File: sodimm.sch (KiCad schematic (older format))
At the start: 1 part, among them J5 2309409-1

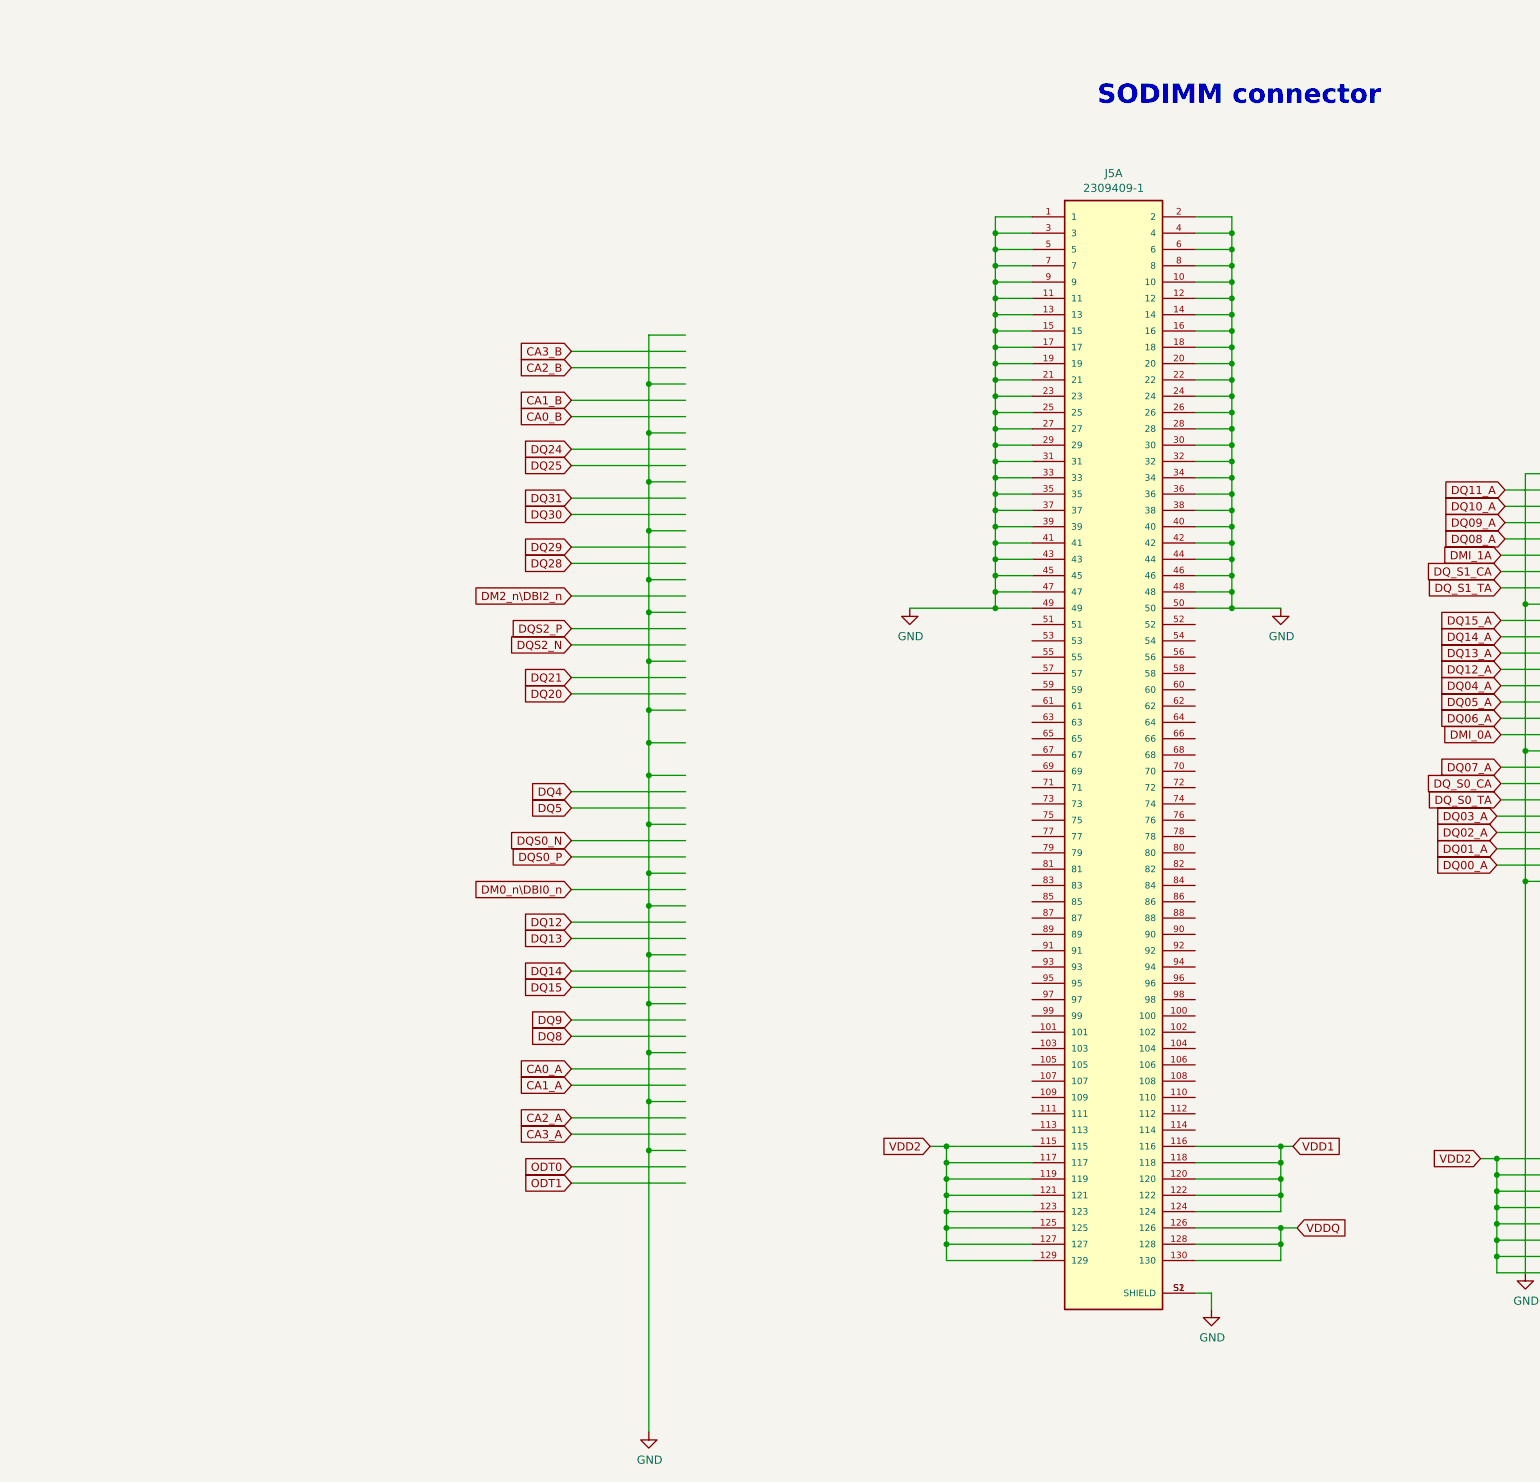
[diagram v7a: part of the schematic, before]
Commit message: Remove redundant signals from the SODIMM
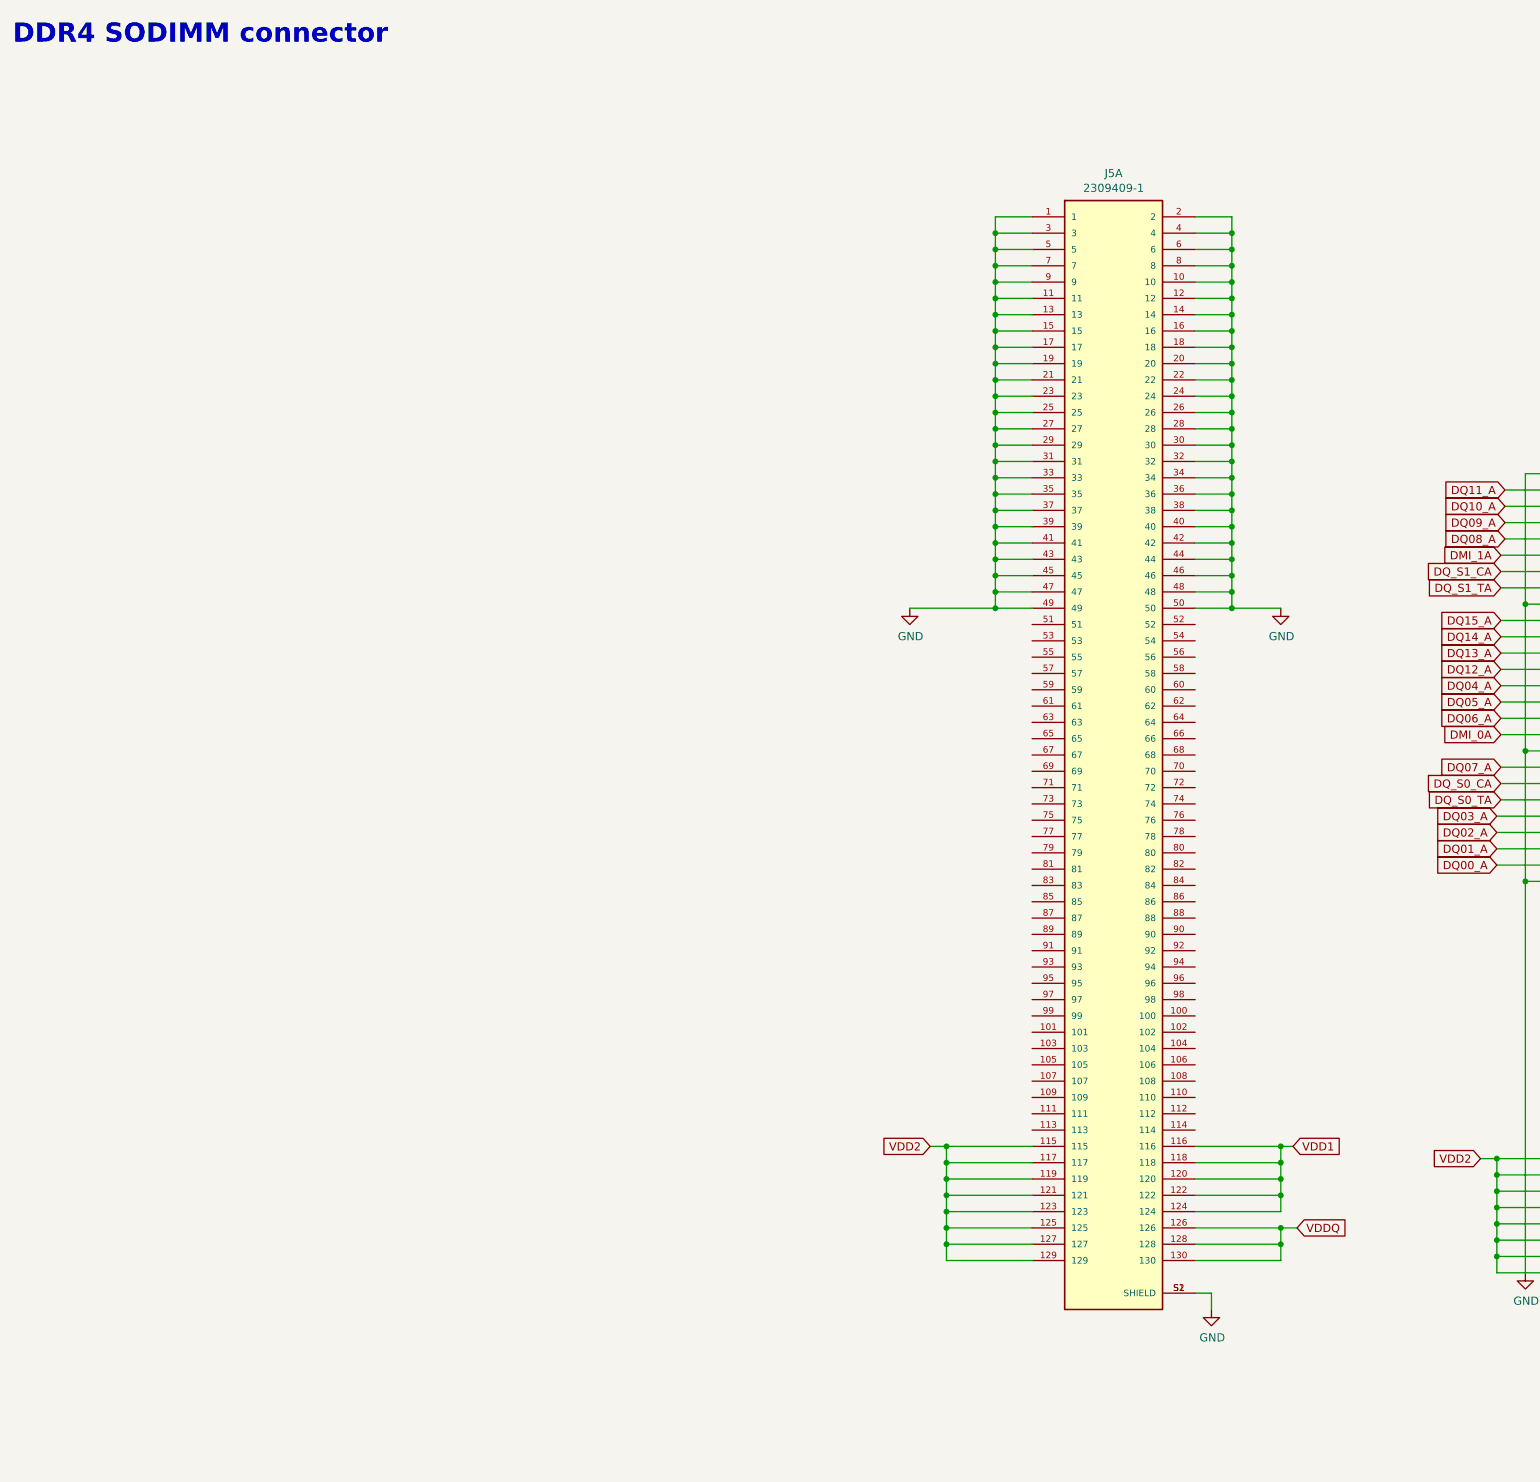
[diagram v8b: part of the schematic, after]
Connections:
- net labels removed: CA0_A, CA0_B, CA1_A, CA1_B, CA2_B, CA3_B, DM0_n\DBI0_n, DM2_n\DBI2_n, DQ12, DQ13, DQ14, DQ15, DQ20, DQ21, DQ24, DQ25, DQ28, DQ29, DQ30, DQ31, DQ4, DQ5, DQ8, DQ9, DQS0_N, DQS0_P, DQS2_N, DQS2_P, ODT0, ODT1
- wire segments 297 -> 227
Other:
- note added: "DDR4 SODIMM connector"
- note removed: "SODIMM connector"
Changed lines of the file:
@@
 	1    0    0    -1
 $EndComp
-Wire Wire Line
-	4850 5825 4150 5825
-Wire Wire Line
-	4850 5925 4150 5925
-Wire Wire Line
-	4850 6925 4150 6925
-Wire Wire Line
-	4850 7025 4150 7025
-Wire Wire Line
-	4850 6625 4150 6625
-Wire Wire Line
-	4850 4825 4150 4825
-Wire Wire Line
-	4850 4625 4150 4625
-Wire Wire Line
-	4850 4525 4150 4525
-Wire Wire Line
-	4850 4025 4150 4025
-Wire Wire Line
-	4850 3525 4150 3525
-Wire Wire Line
-	4850 3825 4150 3825
-Wire Wire Line
-	4850 2925 4150 2925
-Text GLabel 4150 5625 0    50   Input ~ 0
-DQ5
-Text GLabel 4150 5825 0    50   Input ~ 0
-DQS0_N
-Text GLabel 4150 5925 0    50   Input ~ 0
-DQS0_P
-Text GLabel 4150 6425 0    50   Input ~ 0
-DQ13
-Text GLabel 4150 6925 0    50   Input ~ 0
-DQ9
-Text GLabel 4150 6725 0    50   Input ~ 0
-DQ15
-Text GLabel 4150 4825 0    50   Input ~ 0
-DQ21
-Text GLabel 4150 4625 0    50   Input ~ 0
-DQS2_N
-Text GLabel 4150 4525 0    50   Input ~ 0
-DQS2_P
-Text GLabel 4150 3525 0    50   Input ~ 0
-DQ25
-Text GLabel 4150 3825 0    50   Input ~ 0
-DQ30
-Text GLabel 4150 4025 0    50   Input ~ 0
-DQ29
-Text GLabel 4150 2925 0    50   Input ~ 0
-CA2_B
-Wire Wire Line
-	4850 7325 4150 7325
-Text GLabel 4150 7325 0    50   Input ~ 0
-CA1_A
-Wire Wire Line
-	4150 5525 4850 5525
-Wire Wire Line
-	4150 6125 4850 6125
-Wire Wire Line
-	4150 6425 4850 6425
-Wire Wire Line
-	4150 6325 4850 6325
-Wire Wire Line
-	4150 6725 4850 6725
-Wire Wire Line
-	4150 4925 4850 4925
-Wire Wire Line
-	4150 4325 4850 4325
-Wire Wire Line
-	4150 4125 4850 4125
-Wire Wire Line
-	4150 3425 4850 3425
-Wire Wire Line
-	4150 3725 4850 3725
-Wire Wire Line
-	4150 3125 4850 3125
-Wire Wire Line
-	4150 7525 4850 7525
-Wire Wire Line
-	4150 7225 4850 7225
-Wire Wire Line
-	4150 3225 4850 3225
-Wire Wire Line
-	4150 2825 4850 2825
-Text GLabel 4150 6325 0    50   Input ~ 0
-DQ12
-Text GLabel 4150 7025 0    50   Input ~ 0
-DQ8
-Text GLabel 4150 6625 0    50   Input ~ 0
-DQ14
-Text GLabel 4150 4925 0    50   Input ~ 0
-DQ20
-Text GLabel 4150 4125 0    50   Input ~ 0
-DQ28
-Text GLabel 4150 3425 0    50   Input ~ 0
-DQ24
-Text GLabel 4150 3725 0    50   Input ~ 0
-DQ31
-Text GLabel 4150 3125 0    50   Input ~ 0
-CA1_B
-Text GLabel 4150 7525 0    50   Input ~ 0
-CA2_A
-Text GLabel 4150 7225 0    50   Input ~ 0
-CA0_A
-Text GLabel 4150 3225 0    50   Input ~ 0
-CA0_B
-Text GLabel 4150 2825 0    50   Input ~ 0
-CA3_B
-Wire Wire Line
-	4850 7625 4150 7625
-Text GLabel 4150 7625 0    50   Input ~ 0
-CA3_A
-Text GLabel 4150 4325 0    50   Input ~ 0
-DM2_n\DBI2_n
-Text GLabel 4150 6125 0    50   Input ~ 0
-DM0_n\DBI0_n
-Text Notes 7375 1325 0    118  ~ 24
-SODIMM connector
-Text GLabel 4150 5525 0    50   Input ~ 0
-DQ4
-Wire Wire Line
-	4150 5625 4850 5625
+Text Notes 725  950  0    118  ~ 24
+DDR4 SODIMM connector
 Wire Wire Line
 	6975 2000 6750 2000
@@
 Wire Wire Line
 	6975 8300 6450 8300
-Wire Wire Line
-	4850 5225 4625 5225
-$Comp
-L lpddr4-test-board:GND #PWR0180
-U 1 1 65590887
-P 4625 9450
-F 0 "#PWR0180" H 4625 9200 50  0001 C CNN
-F 1 "GND" H 4630 9277 50  0000 C CNN
-F 2 "" H 4625 9450 50  0001 C CNN
-F 3 "" H 4625 9450 50  0001 C CNN
-	1    4625 9450
-	1    0    0    -1
-$EndComp
-Wire Wire Line
-	4625 5225 4625 5425
-Wire Wire Line
-	4625 5225 4625 5025
-Wire Wire Line
-	4625 2725 4850 2725
-Connection ~ 4625 5225
-Wire Wire Line
-	4850 3025 4625 3025
-Connection ~ 4625 3025
-Wire Wire Line
-	4625 3025 4625 2725
-Wire Wire Line
-	4850 3625 4625 3625
-Connection ~ 4625 3625
-Wire Wire Line
-	4625 3625 4625 3325
-Connection ~ 4625 3325
-Wire Wire Line
-	4625 3325 4625 3025
-Wire Wire Line
-	4625 3325 4850 3325
-Connection ~ 4625 3925
-Wire Wire Line
-	4625 3925 4625 3625
-Wire Wire Line
-	4625 3925 4850 3925
-Wire Wire Line
-	4850 4225 4625 4225
-Connection ~ 4625 4225
-Wire Wire Line
-	4625 4225 4625 3925
-Wire Wire Line
-	4850 4425 4625 4425
-Connection ~ 4625 4425
-Wire Wire Line
-	4625 4425 4625 4225
-Wire Wire Line
-	4850 4725 4625 4725
-Connection ~ 4625 4725
-Wire Wire Line
-	4625 4725 4625 4425
-Wire Wire Line
-	4850 5025 4625 5025
-Connection ~ 4625 5025
-Wire Wire Line
-	4625 5025 4625 4725
-Wire Wire Line
-	4850 5425 4625 5425
-Connection ~ 4625 5425
-Wire Wire Line
-	4625 5425 4625 5725
-Connection ~ 4625 5725
-Wire Wire Line
-	4625 5725 4625 6025
-Wire Wire Line
-	4625 5725 4850 5725
-Wire Wire Line
-	4850 6025 4625 6025
-Connection ~ 4625 6025
-Wire Wire Line
-	4625 6025 4625 6225
-Wire Wire Line
-	4850 6225 4625 6225
-Connection ~ 4625 6225
-Wire Wire Line
-	4625 6225 4625 6525
-Wire Wire Line
-	4850 6525 4625 6525
-Connection ~ 4625 6525
-Wire Wire Line
-	4625 6525 4625 6825
-Connection ~ 4625 6825
-Wire Wire Line
-	4625 6825 4625 7125
-Wire Wire Line
-	4625 6825 4850 6825
-Connection ~ 4625 7125
-Wire Wire Line
-	4625 7125 4625 7425
-Wire Wire Line
-	4625 7125 4850 7125
-Wire Wire Line
-	4850 7425 4625 7425
-Connection ~ 4625 7425
-Wire Wire Line
-	4625 7425 4625 7725
-Wire Wire Line
-	4850 7725 4625 7725
-Connection ~ 4625 7725
-Wire Wire Line
-	4625 7725 4625 9450
-Text GLabel 4150 7925 0    50   Input ~ 0
-ODT1
-Text GLabel 4150 7825 0    50   Input ~ 0
-ODT0
-Wire Wire Line
-	4150 7825 4850 7825
-Wire Wire Line
-	4850 7925 4150 7925
 Connection ~ 6450 7800
 Wire Wire Line
